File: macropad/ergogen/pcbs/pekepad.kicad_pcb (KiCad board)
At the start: 2 copper layers, 196 x 43.9 mm, 37 parts

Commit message: improvements
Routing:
- net P009: track 0.00 -> 199.3 mm, vias 0 -> 2
- net P031: track 0.00 -> 103.5 mm, vias 0 -> 1
- net P010: track 0.00 -> 103.5 mm, vias 0 -> 1
- net P008: track 0.00 -> 101.1 mm, vias 0 -> 1
- net P106: track 0.00 -> 86.1 mm
- net P111: track 0.00 -> 85.6 mm
- net P104: track 0.00 -> 81.7 mm
- net P011: track 0.00 -> 73.8 mm
- net P113: track 0.00 -> 68.2 mm
- net P115: track 0.00 -> 66.5 mm, vias 0 -> 3
- net P022: track 0.00 -> 66.4 mm, vias 0 -> 1
- net P100: track 0.00 -> 63.3 mm, vias 0 -> 3
- net P029: track 0.00 -> 54.0 mm, vias 0 -> 2
- net P024: track 0.00 -> 50.0 mm
- net P006: track 0.00 -> 42.8 mm
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
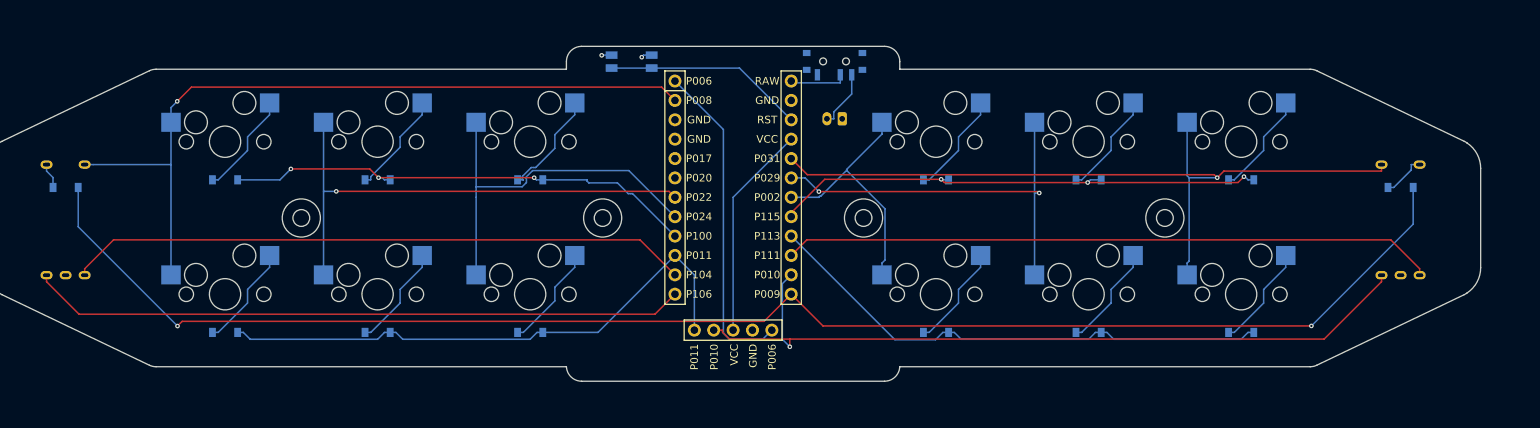
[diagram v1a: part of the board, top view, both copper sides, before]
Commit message: Ajusting plate mcu cutout mcu is now a point of reference
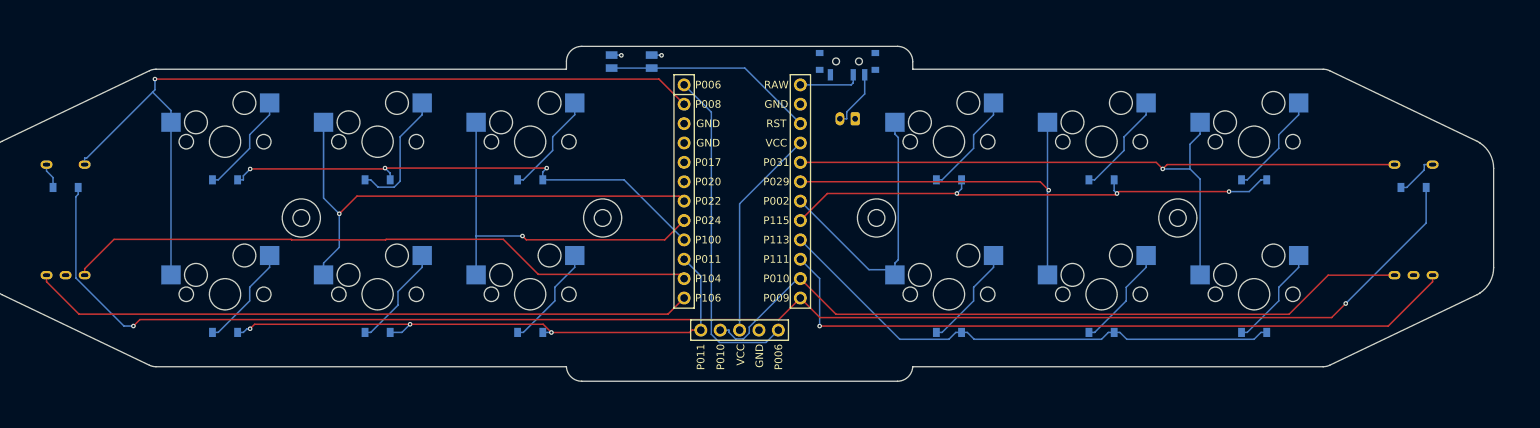
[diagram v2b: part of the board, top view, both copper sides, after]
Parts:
- moved D10 1.70 mm to (214.9, 105.0)
- moved D11 1.70 mm to (194.9, 125.0)
- moved D12 1.70 mm to (194.9, 105.0)
- moved D14 1.70 mm to (255.8, 106.0)
- moved D7 1.70 mm to (234.9, 125.0)
- moved D8 1.70 mm to (234.9, 105.0)
- moved D9 1.70 mm to (214.9, 125.0)
- moved MH3 1.70 mm to (224.9, 110.0)
- moved MH4 1.70 mm to (185.4, 110.0)
- moved RE2 1.70 mm to (255.8, 110.0)
- moved S10 1.70 mm to (214.9, 100.0)
- moved S11 1.70 mm to (194.9, 120.0)
- moved S12 1.70 mm to (194.9, 100.0)
- moved S7 1.70 mm to (234.9, 120.0)
- moved S8 1.70 mm to (234.9, 100.0)
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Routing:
- net P008: track 101.1 -> 110.9 mm
- net P111: track 85.6 -> 93.4 mm, vias 0 -> 1
- net P010: track 103.5 -> 96.8 mm, vias 1 -> 0
- net P009: track 199.3 -> 204.0 mm
- net P002: track 32.9 -> 36.5 mm
- net P100: track 63.3 -> 66.9 mm
- net middle_top: track 13.6 -> 16.8 mm
- net P011: track 73.8 -> 76.1 mm, vias 0 -> 3
- net P022: track 66.4 -> 68.1 mm
- net P104: track 81.7 -> 83.2 mm
- net P024: track 50.0 -> 48.5 mm, vias 0 -> 1
- net RST: track 26.4 -> 27.8 mm
- net P006: track 42.8 -> 44.1 mm
- net P106: track 86.1 -> 87.1 mm
- net P115: track 66.5 -> 67.5 mm
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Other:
- board size 196 x 43.9 mm -> 197.7 x 43.9 mm
